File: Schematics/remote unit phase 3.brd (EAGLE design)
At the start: 55.9 x 29.8 mm, 18 parts, among them IC4 317T, M1 ARDUINO-PRO-MINI-5.0V, M2 WIRELESS-NRF24L01, X2 22-23-2021

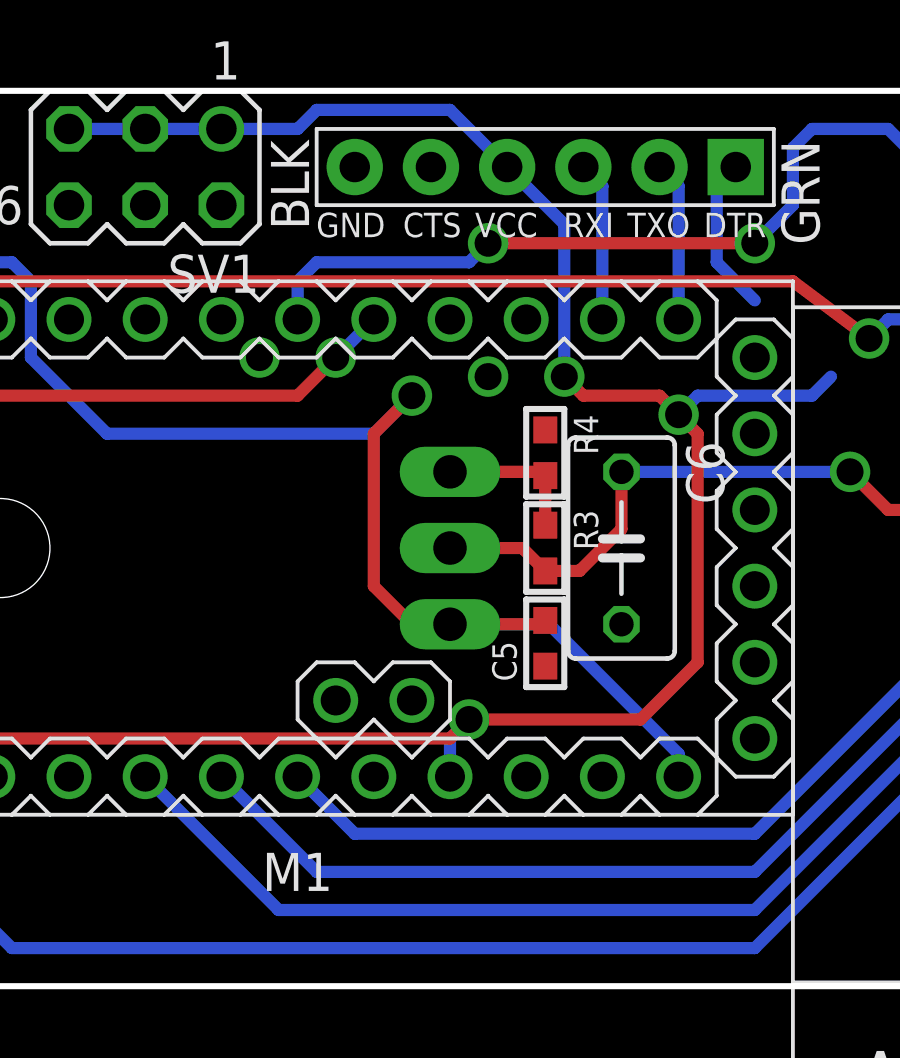
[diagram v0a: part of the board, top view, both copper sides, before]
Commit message: rettelse af sensorafsnit, og sidste schematics
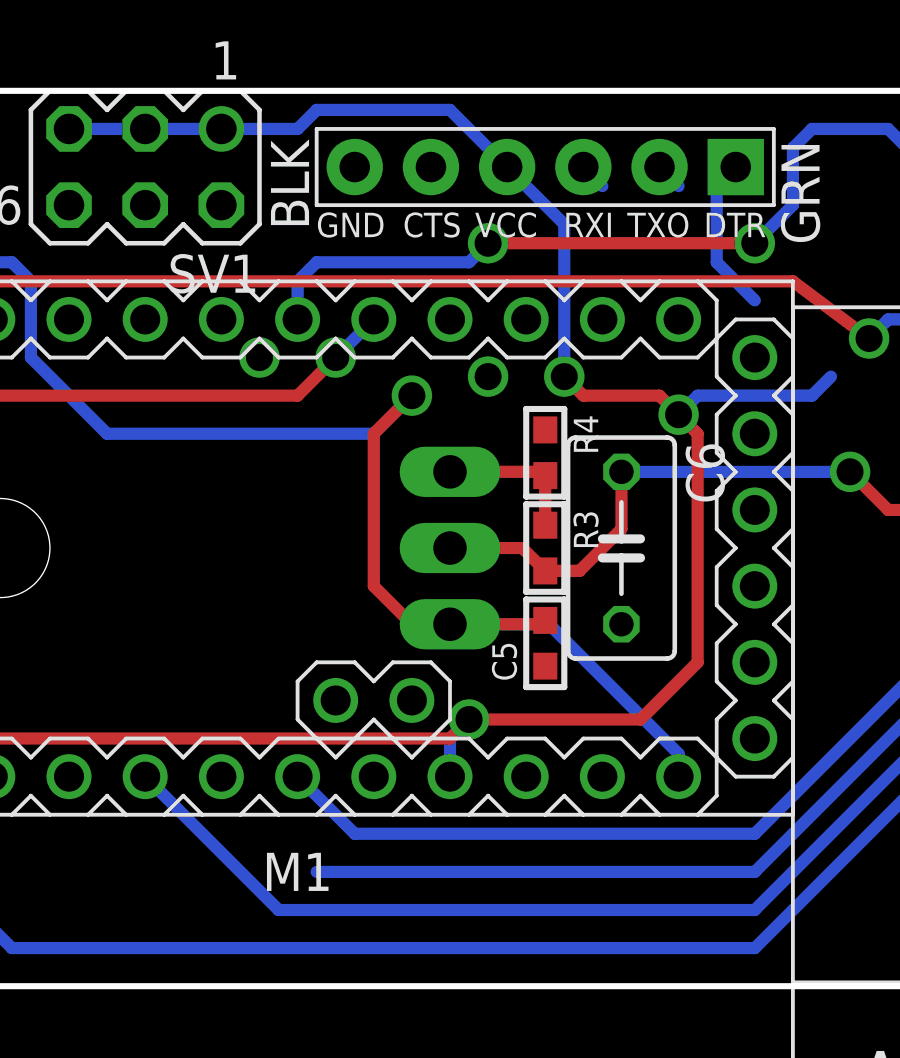
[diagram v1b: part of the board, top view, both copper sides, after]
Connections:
- removed net VCC: U$14.VDD
- net CE: now also M1.J7.6
- net GND: now also U$14.VDD
- net RXI: no longer M1.J7.11
- net TXO: no longer M1.J7.12
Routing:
- net SCK: track 40.2 -> 35.7 mm
- net TXO: track 5.34 -> 0.90 mm
- net RXI: track 5.34 -> 0.90 mm
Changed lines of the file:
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@@
 <via x="24.13" y="19.685" extent="1-16" drill="0.9" shape="octagon"/>
 <via x="16.51" y="20.32" extent="1-16" drill="0.9" shape="octagon"/>
-<wire x1="28.575" y1="11.43" x2="47.625" y2="20.32" width="0" layer="19" extent="1-1"/>
+<contactref element="U$14" pad="VDD"/>
+<wire x1="-2.54" y1="17.78" x2="-139.7" y2="-11.43" width="0" layer="19" extent="1-1"/>
+<wire x1="2.54" y1="13.97" x2="-2.54" y2="17.78" width="0" layer="19" extent="1-1"/>
+<wire x1="3.81" y1="26.035" x2="-2.54" y2="17.78" width="0" layer="19" extent="1-1"/>
+<wire x1="16.51" y1="20.32" x2="3.81" y2="26.035" width="0" layer="19" extent="1-1"/>
+<wire x1="22.86" y1="21.59" x2="16.51" y2="20.32" width="0" layer="19" extent="1-1"/>
+<wire x1="24.13" y1="19.685" x2="22.86" y2="21.59" width="0" layer="19" extent="1-1"/>
+<wire x1="26.035" y1="17.907" x2="24.13" y2="19.685" width="0" layer="19" extent="1-1"/>
+<wire x1="19.685" y1="26.67" x2="22.86" y2="21.59" width="0" layer="19" extent="1-1"/>
+<wire x1="28.575" y1="11.43" x2="26.035" y2="17.907" width="0" layer="19" extent="1-1"/>
 <wire x1="26.035" y1="10.033" x2="28.575" y2="11.43" width="0" layer="19" extent="1-1"/>
 <wire x1="27.94" y1="6.35" x2="26.035" y2="10.033" width="0" layer="19" extent="1-1"/>
-<wire x1="26.035" y1="17.907" x2="28.575" y2="11.43" width="0" layer="19" extent="1-1"/>
-<wire x1="24.13" y1="19.685" x2="26.035" y2="17.907" width="0" layer="19" extent="1-1"/>
-<wire x1="22.86" y1="21.59" x2="24.13" y2="19.685" width="0" layer="19" extent="1-1"/>
-<wire x1="19.685" y1="26.67" x2="22.86" y2="21.59" width="0" layer="19" extent="1-1"/>
-<wire x1="16.51" y1="20.32" x2="22.86" y2="21.59" width="0" layer="19" extent="1-1"/>
-<wire x1="3.81" y1="26.035" x2="16.51" y2="20.32" width="0" layer="19" extent="1-1"/>
-<wire x1="-2.54" y1="17.78" x2="3.81" y2="26.035" width="0" layer="19" extent="1-1"/>
-<wire x1="2.54" y1="13.97" x2="-2.54" y2="17.78" width="0" layer="19" extent="1-1"/>
+<wire x1="47.625" y1="20.32" x2="28.575" y2="11.43" width="0" layer="19" extent="1-1"/>
 </signal>
 <signal name="TXO">
 <contactref element="JP3" pad="P$2"/>
-<contactref element="M1" pad="J7.12"/>
-<wire x1="30.48" y1="21.59" x2="30.48" y2="26.035" width="0.4064" layer="16"/>
 <wire x1="30.48" y1="26.035" x2="29.845" y2="26.67" width="0.4064" layer="16"/>
 </signal>
 <signal name="RXI">
 <contactref element="JP3" pad="P$3"/>
-<contactref element="M1" pad="J7.11"/>
-<wire x1="27.94" y1="21.59" x2="27.94" y2="26.035" width="0.4064" layer="16"/>
 <wire x1="27.94" y1="26.035" x2="27.305" y2="26.67" width="0.4064" layer="16"/>
 </signal>
@@
 <via x="3.175" y="19.685" extent="1-16" drill="0.9" shape="octagon"/>
 <wire x1="3.175" y1="19.685" x2="5.715" y2="19.685" width="0.4064" layer="16"/>
+<contactref element="M1" pad="J7.6"/>
+<wire x1="5.715" y1="19.685" x2="15.24" y2="21.59" width="0" layer="19" extent="16-16"/>
 </signal>
 <signal name="CSN">
@@
 <signal name="SCK">
 <contactref element="M2" pad="5"/>
-<contactref element="M1" pad="J6.7"/>
-<wire x1="15.24" y1="6.35" x2="18.415" y2="3.175" width="0.4064" layer="16"/>
 <wire x1="18.415" y1="3.175" x2="33.02" y2="3.175" width="0.4064" layer="16"/>
 <wire x1="33.02" y1="3.175" x2="41.275" y2="11.43" width="0.4064" layer="16"/>
 <wire x1="41.275" y1="11.43" x2="41.275" y2="19.05" width="0.4064" layer="16"/>
 <wire x1="41.275" y1="19.05" x2="42.545" y2="20.32" width="0.4064" layer="16"/>
+<contactref element="M1" pad="J6.7"/>
+<wire x1="15.24" y1="6.35" x2="18.415" y2="3.175" width="0" layer="19" extent="16-16"/>
 </signal>
 <signal name="MOSI">
@@
 <contactref element="SV1" pad="2"/>
 </signal>
-<signal name="VCC">
-<contactref element="U$14" pad="VDD"/>
-</signal>
 </signals>
